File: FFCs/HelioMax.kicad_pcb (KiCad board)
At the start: 2 copper layers, 249.5 x 156.3 mm, 73 parts, among them J1 Conn_01x01_Pin, J10 Conn_01x07, J11 Conn_01x07, J12 Conn_Telorum_Belt, J13 Conn_to_Telorum_Belt, J4 Conn_C_to_Praetor_Enclave, J5 Conn_R_to_Praetor_Enclave, J6 Conn_01x07, J7 Conn_01x07, J8 Conn_to_Pollex_Cluster, J9 Conn_Pollex_Cluster, SW0:10 SW0:3, SW0:11 SW0:2, SW0:12 SW0:1, SW0:7 SW0:6, SW0:8 SW0:5, SW0:9 SW0:4, SW1:10 SW1:3, SW1:11 SW1:2, SW1:12 SW1:1, SW1:13 SW1:0, SW1:9 SW1:4, SW2:10 SW2:3, SW2:11 SW2:2, SW2:12 SW2:1, SW2:13 SW2:0, SW2:7 SW2:6, SW2:8 SW2:5, SW2:9 SW2:4, SW3:10 SW3:3, SW3:11 SW3:2, SW3:12 SW3:1, SW3:13 SW3:0, SW3:8 SW3:5, SW3:9 SW3:4, SW4:10 SW4:3, SW4:11 SW4:2, SW4:12 SW4:1, SW4:13 SW4:0, SW4:7 SW4:6, SW4:8 SW4:5, SW4:9 SW4:4, SW5:10 SW5:3, SW5:11 SW5:2, SW5:12 SW5:1, SW5:13 SW5:0, SW5:7 SW5:6, SW5:8 SW5:5, SW5:9 SW5:4, SW6:10 SW6:3, SW6:11 SW6:2, SW6:12 SW6:1, SW6:13 SW6:0, SW6:7 SW6:6, SW6:8 SW6:5, SW6:9 SW6:4

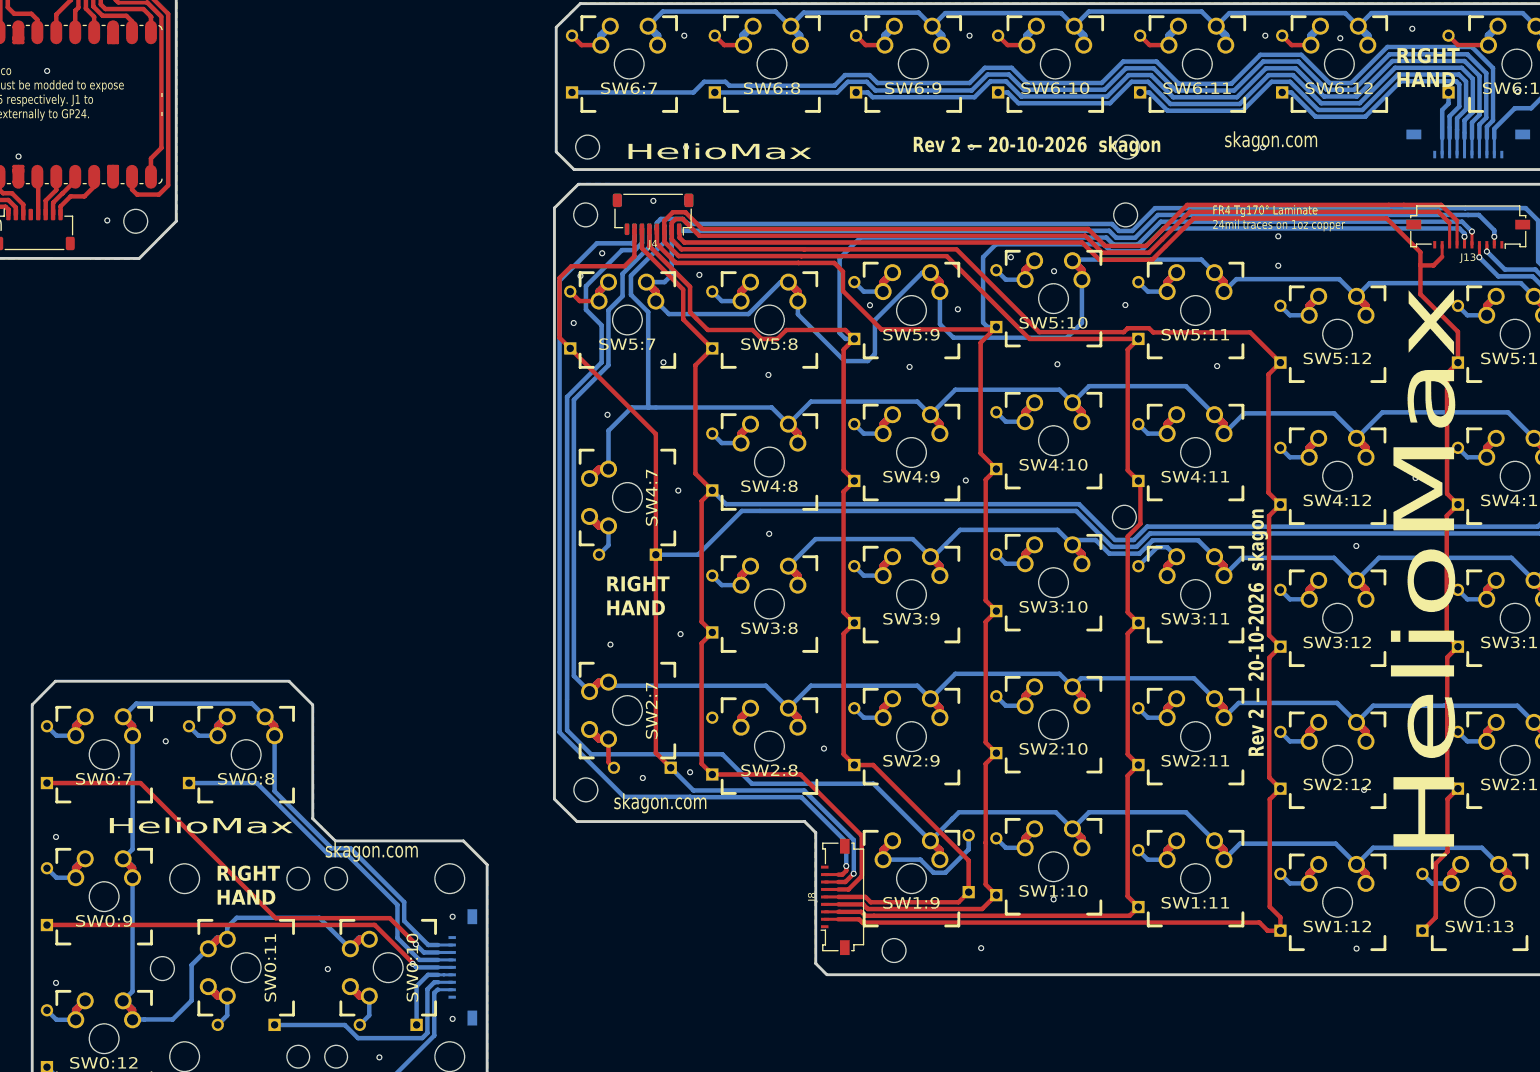
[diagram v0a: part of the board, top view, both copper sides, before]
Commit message: Eliminated two vias in Pollex Cluster. Some minor wiring cleanup.
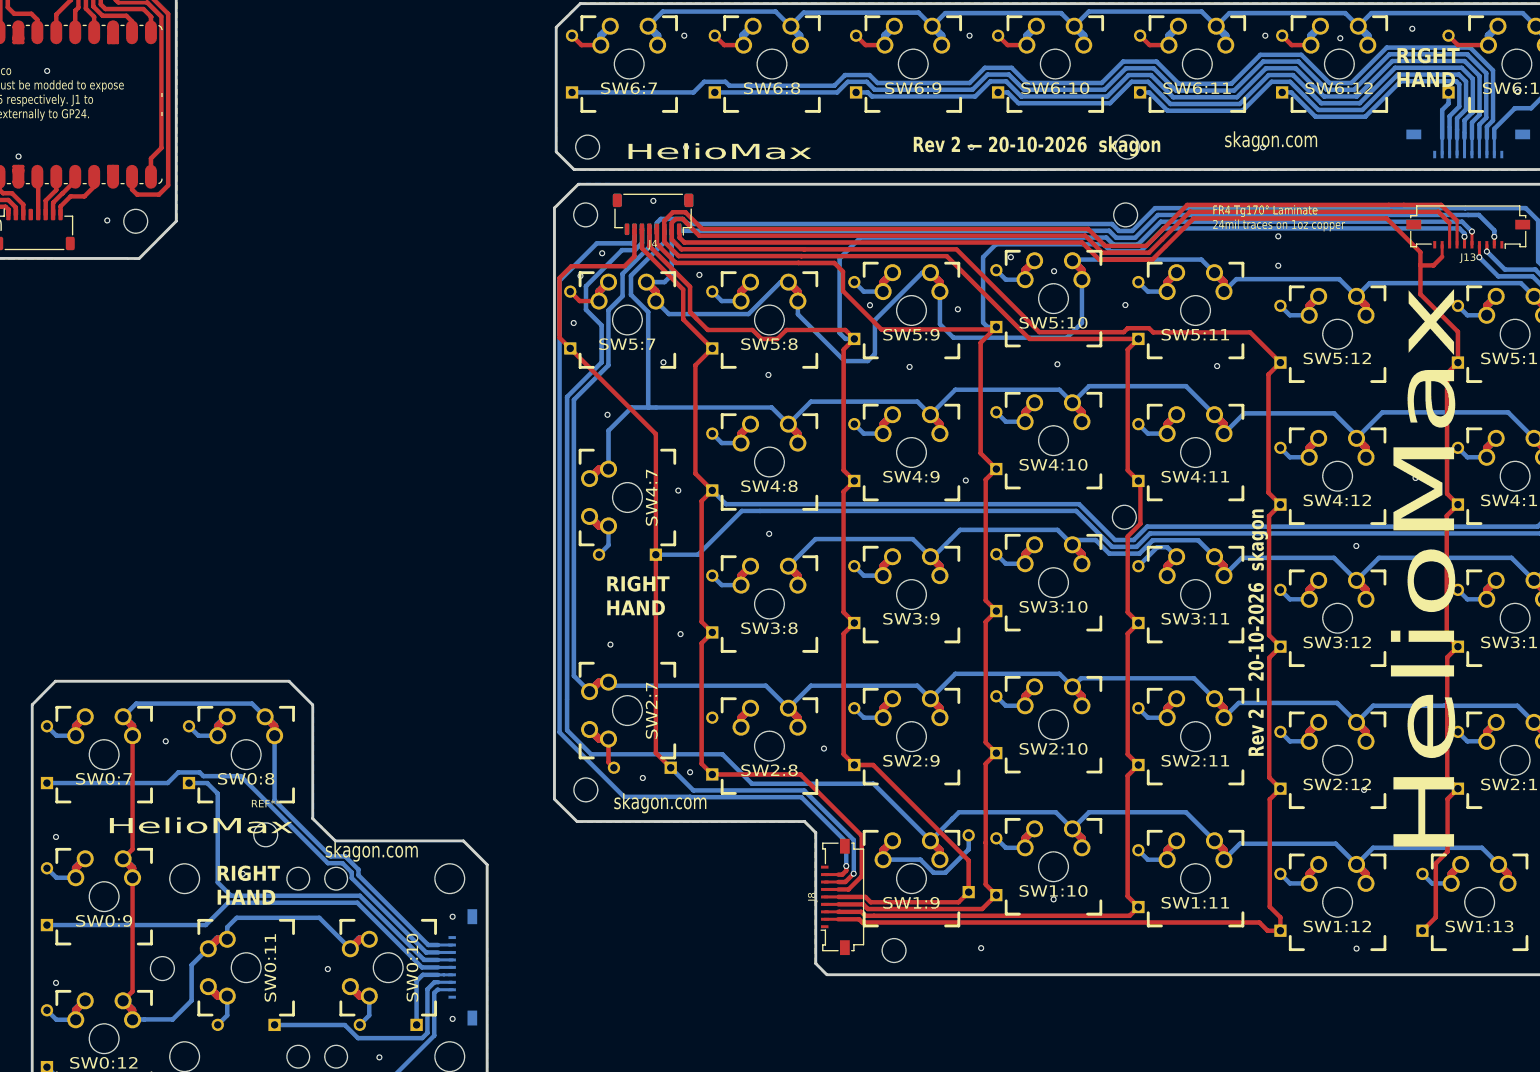
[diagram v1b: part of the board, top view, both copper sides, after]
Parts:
- added REF**: MountingHole_3.2mm_M3, MountingHole:MountingHole_3.2mm_M3, F.Cu at (91.7, 143.3)
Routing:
- net /COL5: track 451.0 -> 455.3 mm
- net /COL4: track 407.8 -> 410.2 mm, vias 2 -> 1
- net /COL6: track 507.4 -> 508.8 mm, vias 3 -> 2
- net GND: vias 62 -> 63
